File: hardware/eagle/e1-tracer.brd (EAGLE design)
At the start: 160 x 120 mm, 108 parts, among them IC1 W25Q80DVSNIG, IC2 MCP1703T-1202E/CB, IC3 TPS73633DCQR, IC4 ASEM1-12.000MHZ-LC-T, J1 PASSTHROUGH, M1 MENTOR_12701001, M2 MENTOR_12701001, T1 BC847C, T2 BC847C, U1 ICE40UP5K-SG48I, U2 IP4234CZ6, U3 IDT82V2081, U4 IDT82V2081, U5 2.048 Mhz, U6 1.544 MHz, X1 MINI-USB-SHIELD-UX60-MB-5ST

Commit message: e1-tracer: finish PCB
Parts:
- removed B1: (no value), microbuilder:EVQ-Q2
- removed C15: 10n, rc-sysmocom:_0603@1
- removed IC3: TPS73633DCQR, laforge:SOT223-6
- removed JP2: TCLK/MCLK, jumper:JP1
- removed JP3: 1544/2048, jumper:JP2
- removed R7: 2.2k, rc-sysmocom:_0402
- added IC5: TLV70233DBVR, tlv700xx:SOT23-DBV
- added R38: 1k, rc-sysmocom:_0603
- added R39, R40, R41: DNP, rc-sysmocom:_0603
- added SW1: TACTSW-TL3340, tact-switches:TL3340-ORIG
- added U$1, U$3: (no value), oshw:OSHW_8MM_COPPER
- added U7: 1.544 MHz, laforge:HC73
- added X2: JACK2.5_SJ-2523, laforge:JACK2.5_SJ-2523
- C11: value 1u -> 22u; device rc-sysmocom:_0603@1 -> rc-sysmocom:1206@1
- C12: value 10n -> 1u; device rc-sysmocom:_0402@1 -> rc-sysmocom:_0603@1
- C13: value 100n -> 10n; device rc-sysmocom:_0603@1 -> rc-sysmocom:_0402@1
- C14: value 22u -> 100n; device rc-sysmocom:1206@1 -> rc-sysmocom:_0603@1
- IC1: value W25Q80DVSNIG -> MCP1703T-1202E/CB; device spiflash:SO08COMBINED -> MCP170x:SOT23-3
- IC2: value MCP1703T-1202E/CB -> W25Q80DVSNIG; device MCP170x:SOT23-3 -> spiflash:SO08COMBINED
- LOS1, LOS2: value RED -> LEDPLCC2-MIN-red; device led:CHIPLED_0805 -> LED-PLCC2:PLCC2-MIN
- PWR: value GREEN -> LEDPLCC2-MIN-green; device led:CHIPLED_0805 -> LED-PLCC2:PLCC2-MIN
- R10: value 10k -> 68
- R28: value 3k 1% -> 10k
- R30: value 10k -> 3k 1%
- R32: value 120 -> 10k
- R34: value 68 -> 120
- R35: value 68 -> 330
- R36: value 1k -> 330
- R8: value 10k -> 2.2k; device rc-sysmocom:_0603 -> rc-sysmocom:_0402
- R9: value 68 -> 10k
- U3: value IDT82V2081 -> IP4234CZ6; device laforge:TQFP44 -> laforge:TSOP-6
- U5: value 2.048 Mhz -> IDT82V2081; device laforge:HC73 -> laforge:TQFP44
- U6: value 1.544 MHz -> 2.048 Mhz
- moved U5 85.4 mm to (65.4, 62.9)
- moved R29 84.8 mm to (42.9, 55.2), turned to 180 degrees
- moved U4 84.5 mm to (36.2, 62.9)
- moved R36 83.9 mm to (10.8, 23.2)
- moved R32 82.0 mm to (11.7, 30.8), turned to 90 degrees
- moved R18 72.9 mm to (24.8, 64.1), turned to 180 degrees
- moved R27 72.9 mm to (54.0, 64.1), turned to 180 degrees
- moved R10 71.8 mm to (23.8, 11.1), turned to 90 degrees
- moved R37 71.8 mm to (39.4, 20.4)
- moved R33 70.2 mm to (38.4, 35.0)
- moved R19 69.3 mm to (41.9, 72.4), turned to 90 degrees
- moved C12 69.0 mm to (72.7, 12.9)
- moved R8 66.5 mm to (73.7, 18.1)
- moved U6 61.6 mm to (89.9, 54.6)
- moved C16 60.8 mm to (90.5, 19.7), turned to 90 degrees
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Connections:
- removed net N$4 (its old number): R28.2, U3.43
- new net N$1: R30.2, U5.43
- new net UART_TX0: U3.1, X2.3
- new net VDD: U3.5
- net BOOT_SW: now also SW1.2; no longer B1.A, B1.A'
- net CDONE: now also R8.2; no longer R7.2
- net GND: now also IC1.1, IC2.4, IC5.2, IC5.4, R18.2, R27.2, R30.1, R40.2, R41.1, SW1.1, SW1.3, U3.2, U5.10, U5.11, U5.13, U5.14, U5.15, U5.17, U5.18, U5.22, U5.38, U5.39, U7.P$2, X2.1; no longer B1.B, B1.B', C15.2, IC1.4, IC2.1, IC3.3, IC3.6, JP3.2, R19.2, R28.1, R9.2, U3.10, U3.11, U3.13, U3.14, U3.15, U3.17, U3.18, U3.22, U3.38, U3.39, U5.P$2
- net IOB_32A_SPI_SO: now also IC2.2; no longer IC1.2
- net IOB_33B_SPI_SI: now also IC2.5; no longer IC1.5
- net IOB_34A_SPI_SCK: now also IC2.6; no longer IC1.6
- net IOB_35B_SPI_SS: now also IC2.1; no longer IC1.1
- net IO_A0: now also U5.24; no longer U3.24
- net IO_A1: now also U5.23; no longer U3.23
- net IO_A2: now also U5.25; no longer U3.25
- net IO_A3: now also U3.3
- net IO_A4: now also U4.21; no longer U3.21
- net IO_A5: now also U5.21; no longer U4.21
- net IO_B0: now also U4.4; no longer U3.4
- net IO_B1: now also U4.5; no longer U3.5
- net IO_B2: now also U5.4; no longer U4.4
- net IO_B3: now also U5.5; no longer U4.5
- net LOS0: now also R31.2, U4.7; no longer R30.2, U3.7
- net LOS1: now also R32.2, U5.7; no longer R31.2, U4.7
- net MCLK: now also R39.2, U5.9, U7.P$3; no longer JP2.1, U3.9, U5.P$3
- net N$10: now also R13.1, U4.31; no longer R12.1, U3.31
- net N$11: now also R14.1, U4.30; no longer R13.1, U3.30
- net N$12: now also R15.1, U4.29; no longer R14.1, U3.29
- net N$13: now also R16.1, U4.28; no longer R15.1, U3.28
- net N$14: now also R17.1, U4.27; no longer R16.1, U3.27
- net N$15: now also R22.1, U5.31; no longer R21.1, U4.31
- net N$16: now also R23.1, U5.30; no longer R22.1, U4.30
- net N$17: now also R19.1, U4.12; no longer R18.1, U3.12
- net N$18: now also R18.1, U4.26; no longer R17.1, U3.26
- net N$19: now also R24.1, U5.29; no longer R23.1, U4.29
- net N$2: now also R28.1, U5.12; no longer R27.1, U4.12
- net N$20: now also R25.1, U5.28; no longer R24.1, U4.28
- net N$21: now also R26.1, U5.27; no longer R25.1, U4.27
- net N$22: now also R27.1, U5.26; no longer R26.1, U4.26
- net N$23: now also U4.42; no longer U3.42
- net N$25: now also R9.1; no longer R8.1
- net N$26: now also R31.1; no longer R30.1
- net N$27: now also LOS1.K, R35.1; no longer LOS1.C, R34.1
- net N$28: now also R35.2; no longer R34.2
- net N$29: now also PWR.K, R10.1; no longer PWR.C, R9.1
- net N$3: now also U5.42; no longer U4.42
- net N$30: now also R37.1; no longer R36.1
- net N$31: now also R32.1; no longer R31.1
- net N$35: now also R40.1, U6.P$1; no longer JP3.3, U5.P$1
- net N$36: now also X1.M2, X1.M3; no longer C15.1, IC3.4
- net N$37: now also LOS2.K, R36.1; no longer LOS2.C, R35.1
- net N$38: now also R41.2, U7.P$1; no longer JP3.1, U6.P$1
- net N$39: now also R36.2; no longer R35.2
- net N$41: now also R38.1; no longer R37.1
- net N$42: now also R37.2; no longer R36.2
- net N$5: now also R38.2; no longer R37.2
- net N$6: now also R20.1, U5.33; no longer R19.1, U4.33
- net N$61: now also C13.1; no longer C12.1
- net N$7: now also R21.1, U5.32; no longer R20.1, U4.32
- net N$8: now also R11.1, U4.33; no longer R10.1, U3.33
- net N$9: now also R12.1, U4.32; no longer R11.1, U3.32
- net RRING: now also R33.1, U4.40; no longer R32.1, U3.40
- net RRING1: now also R34.1, U5.40; no longer R33.1, U4.40
- net RTIP: now also R33.2, U4.41; no longer R32.2, U3.41
- net RTIP1: now also R34.2, U5.41; no longer R33.2, U4.41
- net TCLK: now also R39.1, U5.1; no longer JP2.2, U3.1
- net VBUS: now also C11.1, C12.1, IC1.3, IC5.1; no longer C10.1, C14.1, IC2.3, IC3.1
- net VCC_1V2: now also C10.1, IC1.2, IC5.3; no longer C11.1, IC2.2, IC3.5
- net VCC_3V3: now also C14.1, IC2.3, IC2.7, IC2.8, IC5.5, R19.2, R28.2, R8.1, R9.2, U5.16, U5.19, U5.35, U5.8, U7.P$4; no longer C13.1, IC1.3, IC1.7, IC1.8, IC3.2, R18.2, R27.2, R7.1, R8.2, U3.16, U3.19, U3.35, U3.8, U5.P$4
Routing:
- net N$64: track 20.2 -> 69.8 mm, vias 1 -> 2
- net N$63: track 24.0 -> 73.2 mm, vias 1 -> 2
- net N$65: track 21.4 -> 69.6 mm, vias 1 -> 2
- net IO_A3: track 0.00 -> 25.0 mm, vias 0 -> 2
- net VBUS: track 98.7 -> 78.3 mm
- net VCC_3V3: track 54.0 -> 69.6 mm
- net GND: track 142.1 -> 155.0 mm, vias 74 -> 72
- net UART_TX0: track 0.00 -> 12.2 mm
- net BOOT_SW: track 27.6 -> 38.3 mm, vias 2 -> 4
- net N$1: track 0.00 -> 6.02 mm
- net VCC_1V2: track 82.4 -> 87.9 mm, vias 4 -> 6
- net MCLK: track 64.0 -> 59.0 mm
- net N$4 (its old number): track 4.17 -> 0.00 mm
- net N$35: track 16.6 -> 12.9 mm, vias 1 -> 2
- net N$38: track 17.3 -> 14.0 mm, vias 1 -> 0
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- removed copper zone on layer 1, net GND
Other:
- board size 160 x 120 mm -> 100 x 75 mm
- board text added: "OSHW / CC-BY-SA"

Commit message: e1-tracer: 'update' our generic rc lib again to purge '..@1' packages
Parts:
- C1, C10, C12, C14, C17, C18, C19, C2, C20, C21, C22, C23, C24, C25, C26, C27, C28, C29, C3, C4, C5, C6, C7, C8, C9: device rc-sysmocom:_0603@1 -> rc-sysmocom:_0603
- C11, C16: device rc-sysmocom:1206@1 -> rc-sysmocom:1206
- C13: device rc-sysmocom:_0402@1 -> rc-sysmocom:_0402

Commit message: e1-tracer: reapir missing VDD_3V3 on serial debug out's TVS
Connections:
- removed net VDD: U3.5
- net VCC_3V3: now also U3.5
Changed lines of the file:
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@@
 <layer number="20" name="Dimension" color="15" fill="1" visible="yes" active="yes"/>
 <layer number="21" name="tPlace" color="7" fill="1" visible="yes" active="yes"/>
-<layer number="22" name="bPlace" color="7" fill="1" visible="no" active="yes"/>
+<layer number="22" name="bPlace" color="7" fill="1" visible="yes" active="yes"/>
 <layer number="23" name="tOrigins" color="15" fill="1" visible="yes" active="yes"/>
 <layer number="24" name="bOrigins" color="15" fill="1" visible="no" active="yes"/>
@@
 <layer number="27" name="tValues" color="7" fill="1" visible="no" active="yes"/>
 <layer number="28" name="bValues" color="7" fill="1" visible="no" active="yes"/>
-<layer number="29" name="tStop" color="7" fill="3" visible="no" active="yes"/>
+<layer number="29" name="tStop" color="7" fill="3" visible="yes" active="yes"/>
 <layer number="30" name="bStop" color="7" fill="6" visible="no" active="yes"/>
 <layer number="31" name="tCream" color="7" fill="4" visible="no" active="yes"/>
@@
 <attribute name="ROHSCERTIFICATE" value="Bleifrei / RoHS-konform" x="76.2" y="37.56" size="1.778" layer="27" rot="R180" display="off"/>
 <attribute name="DESCRIPTION" value="CAP CER 0.1UF 16V 10% X7R 0603" x="76.2" y="37.56" size="1.778" layer="27" rot="R180" display="off"/>
-<attribute name="NAME" x="81.5975" y="37.2425" size="1.1" layer="25" font="vector" ratio="16"/>
+<attribute name="NAME" x="77.62875" y="36.925" size="1.1" layer="25" font="vector" ratio="16"/>
 <attribute name="VALUE" x="77.7875" y="39.0523" size="1.1" layer="27" font="vector" ratio="16" rot="R180"/>
 </element>
@@
 <attribute name="ROHSCERTIFICATE" value="Bleifrei / RoHS-konform" x="76.2" y="38.83" size="1.778" layer="27" rot="R180" display="off"/>
 <attribute name="DESCRIPTION" value="CAP CER 1UF 10V X5R 0603" x="76.2" y="38.83" size="1.778" layer="27" rot="R180" display="off"/>
-<attribute name="NAME" x="81.5975" y="38.5125" size="1.1" layer="25" font="vector" ratio="16"/>
+<attribute name="NAME" x="78.9625" y="38.1" size="1.1" layer="25" font="vector" ratio="16" rot="R90"/>
 <attribute name="VALUE" x="77.7875" y="40.3223" size="1.1" layer="27" font="vector" ratio="16" rot="R180"/>
 </element>
@@
 <wire x1="71.12" y1="36.29" x2="72.7075" y2="36.29" width="0.4064" layer="16"/>
 <wire x1="72.7075" y1="36.29" x2="72.86625" y2="36.44875" width="0.4064" layer="16"/>
+<contactref element="U3" pad="5"/>
 </signal>
 <signal name="VBUS" class="1">
@@
 <wire x1="64.9925" y1="14.8275" x2="64.9925" y2="14.925" width="0.3048" layer="1"/>
 </signal>
-<signal name="VDD" class="2">
-<contactref element="U3" pad="5"/>
-</signal>
 <signal name="N$36">

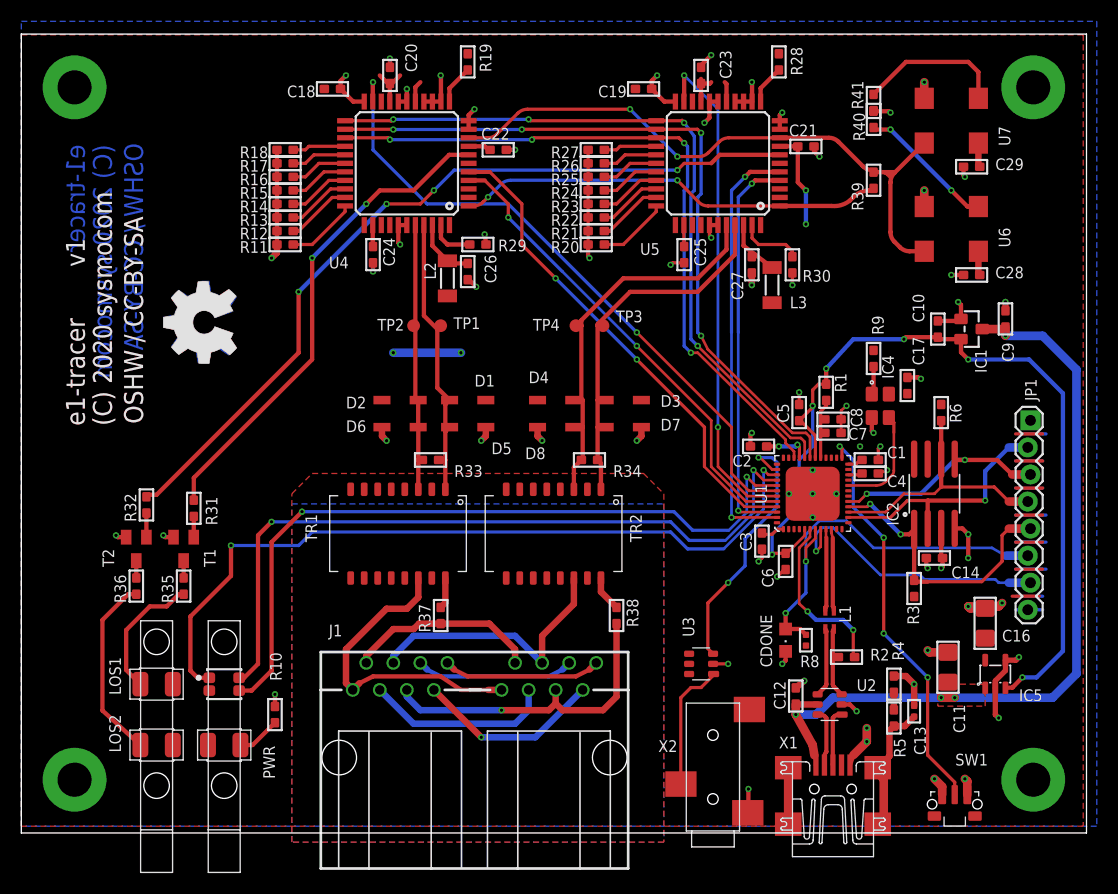
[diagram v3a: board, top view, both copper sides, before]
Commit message: e1-tracer: add 2x 33R series resistors in USB wires
and
* update improved HC73 package
* move upper third of PCB (LIUs and XOs) left
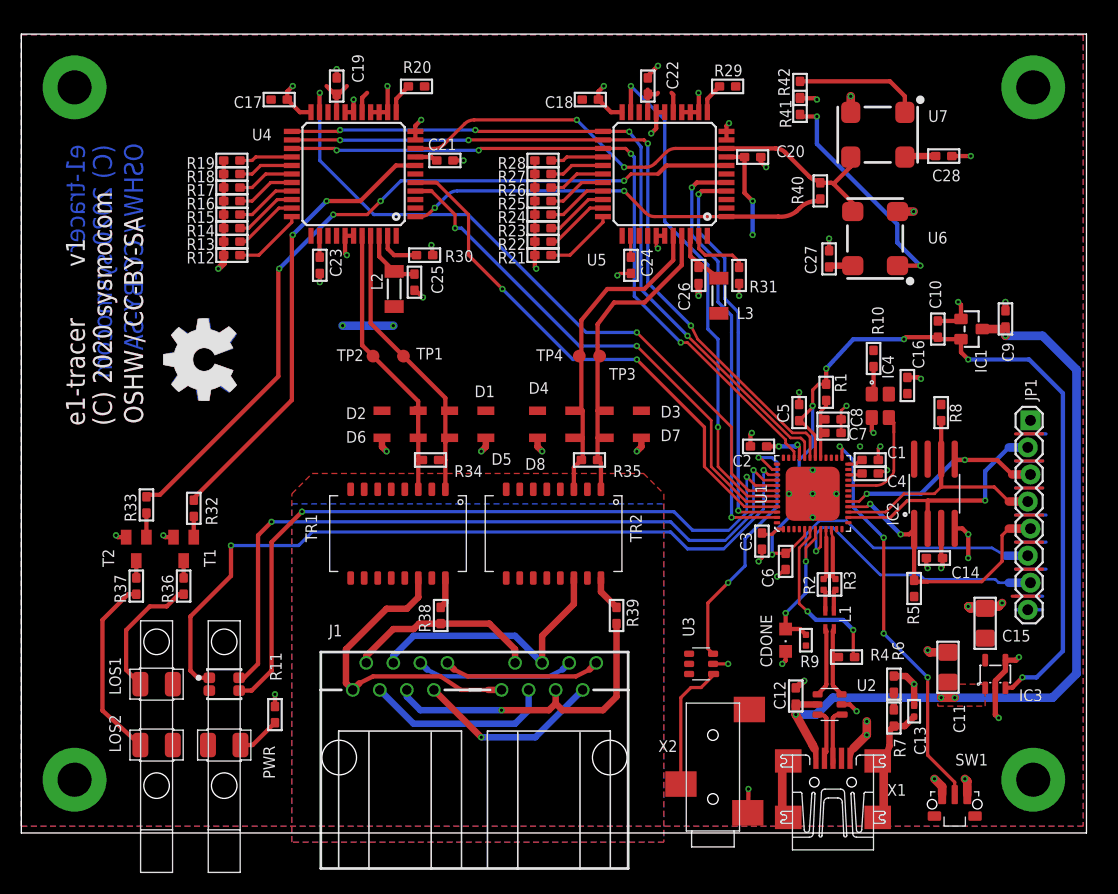
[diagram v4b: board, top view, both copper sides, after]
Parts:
- removed C29: 100n, rc-sysmocom:_0603
- added C15: 22u, rc-sysmocom:1206
- added R42: DNP, rc-sysmocom:_0603
- added R7: 100k, rc-sysmocom:_0603
- C16: value 22u -> 100n; device rc-sysmocom:1206 -> rc-sysmocom:_0603
- C17: value 100n -> 68µ DNP
- C19: value 68µ DNP -> 100n
- R10: value 68 -> 10k
- R11: value 10k -> 68
- R2: value 1k5 -> 33; device rc-sysmocom:_0603 -> rc-sysmocom:_0402
- R29: value 3k 1% -> 10k
- R3: value 10k -> 33; device rc-sysmocom:_0603 -> rc-sysmocom:_0402
- R31: value 10k -> 3k 1%
- R33: value 120 -> 10k
- R35: value 330 -> 120
- R37: value 1k -> 330
- R39: value DNP -> 1k
- R4: value 100k -> 1k5
- R5: value 100k -> 10k
- R6: value 10k -> 100k
- R8: value 2.2k -> 10k; device rc-sysmocom:_0402 -> rc-sysmocom:_0603
- R9: value 10k -> 2.2k; device rc-sysmocom:_0603 -> rc-sysmocom:_0402
- moved R10 65.4 mm to (80.0, 44.5)
- moved C17 64.8 mm to (24.2, 68.8), turned to 180 degrees
- moved R31 55.7 mm to (67.4, 52.3)
- moved R39 47.5 mm to (55.9, 20.4)
- moved R11 44.1 mm to (23.8, 11.1), turned to 90 degrees
- moved C23 40.0 mm to (28.0, 53.3), turned to 270 degrees
- moved R35 39.9 mm to (53.3, 35.0), turned to 0 degrees
- moved C20 34.9 mm to (68.7, 63.5), turned to 0 degrees
- moved R30 34.5 mm to (37.9, 54.2), turned to 180 degrees
- moved C21 33.9 mm to (39.8, 63.1)
- moved C19 28.8 mm to (29.6, 70.1), turned to 90 degrees
- moved R37 28.7 mm to (10.8, 23.2)
- moved R29 27.8 mm to (66.3, 70.1), turned to 0 degrees
- moved R9 27.2 mm to (73.7, 18.1)
- moved R33 27.0 mm to (11.7, 30.8), turned to 90 degrees
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- renumbered IC5 to IC3
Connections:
- new net _D_N: L1.4, R2.2
- new net _D_P: L1.1, R3.2
- net CDONE: now also R9.2; no longer R8.2
- net GND: now also C15.2, C17.1, C19.2, C27.1, R19.2, R28.2, R31.1, R41.2, R42.1, R6.1; no longer C17.2, C19.1, C27.2, C29.1, R10.2, R20.2, R29.1, R4.1, R40.2, R41.1
- net IOB_34A_SPI_SCK: now also R8.1; no longer R6.1
- net IOB_35B_SPI_SS: now also R5.1; no longer R3.1
- net LOS0: now also R32.2; no longer R31.2
- net LOS1: now also R33.2; no longer R32.2
- net MCLK: now also R40.2; no longer R39.2
- net N$1: now also R31.2; no longer R30.2
- net N$10: now also R14.1; no longer R13.1
- net N$11: now also R15.1; no longer R14.1
- net N$12: now also R16.1; no longer R15.1
- net N$13: now also R17.1; no longer R16.1
- net N$14: now also R18.1; no longer R17.1
- net N$15: now also R23.1; no longer R22.1
- net N$16: now also R24.1; no longer R23.1
- net N$17: now also R20.1; no longer R19.1
- net N$18: now also R19.1; no longer R18.1
- net N$19: now also R25.1; no longer R24.1
- net N$2: now also R29.1; no longer R28.1
- net N$20: now also R26.1; no longer R25.1
- net N$21: now also R27.1; no longer R26.1
- net N$22: now also R28.1; no longer R27.1
- net N$23: now also C25.1; no longer C26.1
- net N$25: now also R10.1; no longer R9.1
- net N$26: now also R32.1; no longer R31.1
- net N$27: now also R36.1; no longer R35.1
- net N$28: now also R36.2; no longer R35.2
- net N$29: now also R11.1; no longer R10.1
- net N$3: now also C26.1; no longer C27.1
- net N$30: now also R38.1; no longer R37.1
- net N$31: now also R33.1; no longer R32.1
- net N$35: now also R41.1; no longer R40.1
- net N$37: now also R37.1; no longer R36.1
- net N$38: now also R42.2; no longer R41.2
- net N$39: now also R37.2; no longer R36.2
- net N$4: now also R30.2; no longer R29.2
- net N$41: now also R39.1; no longer R38.1
- net N$42: now also R38.2; no longer R37.2
- net N$5: now also R39.2; no longer R38.2
- net N$55: now also R6.2, R7.1; no longer R4.2, R5.1
- net N$6: now also R21.1; no longer R20.1
- net N$61: now also R7.2; no longer R5.2
- net N$7: now also R22.1; no longer R21.1
- net N$8: now also R12.1; no longer R11.1
- net N$9: now also R13.1; no longer R12.1
- net RRING: now also R34.1; no longer R33.1
- net RRING1: now also R35.1; no longer R34.1
- net RTIP: now also R34.2; no longer R33.2
- net RTIP1: now also R35.2; no longer R34.2
- net TCLK: now also R40.1; no longer R39.1
- net USB1_D_P: now also R4.2; no longer R2.2
- net USB_D_N: now also R2.1; no longer L1.4
- net USB_D_P: now also R3.1; no longer L1.1
- net USB_PU: now also R4.1; no longer R2.1
- net VCC_3V3: now also C15.1, C17.2, C19.1, C27.2, R10.2, R20.2, R29.2, R5.2, R8.2, R9.1; no longer C17.1, C19.2, C25.1, C29.2, R19.2, R28.2, R3.2, R6.2, R8.1, R9.2
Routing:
- net N$35: track 12.9 -> 21.8 mm
- net MCLK: track 59.0 -> 50.4 mm
- net RRING1: track 37.2 -> 31.6 mm
- net RTIP1: track 35.9 -> 30.4 mm
- net IO_B1: track 46.4 -> 51.0 mm
- net IO_B0: track 44.7 -> 49.3 mm
- net IO_A4: track 61.9 -> 66.5 mm
- net LOS0: track 46.0 -> 43.0 mm
- net USB_D_P: track 7.73 -> 4.81 mm
- net USB_D_N: track 7.73 -> 4.80 mm
- net LOS1: track 76.1 -> 73.2 mm
- net _D_N: track 0.00 -> 2.04 mm
- net _D_P: track 0.00 -> 2.04 mm
- net N$38: track 14.0 -> 11.9 mm
- net RRING: track 25.5 -> 26.8 mm
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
